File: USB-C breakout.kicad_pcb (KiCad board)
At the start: 2 copper layers, 14.7 x 21.2 mm, 10 parts, among them J1 USB_C_Receptacle_USB2.0, P1 Conn_01x04_MountingPin

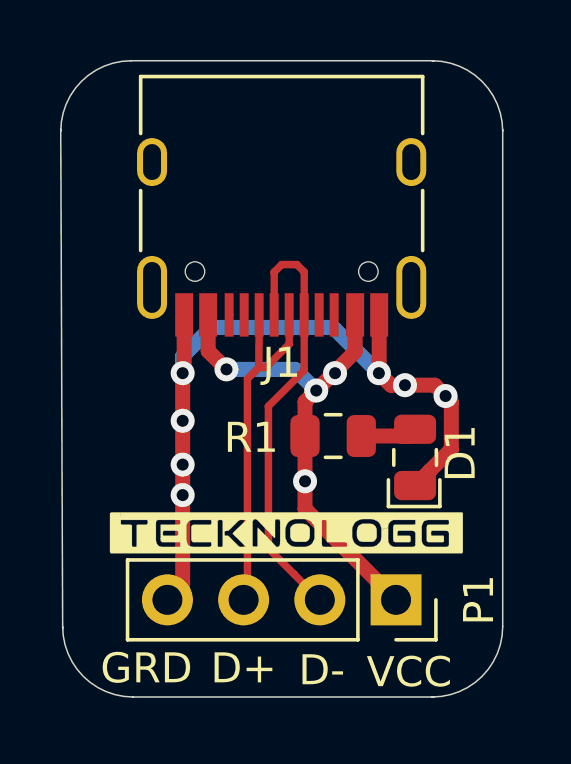
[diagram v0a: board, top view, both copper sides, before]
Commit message: Add CC resistors
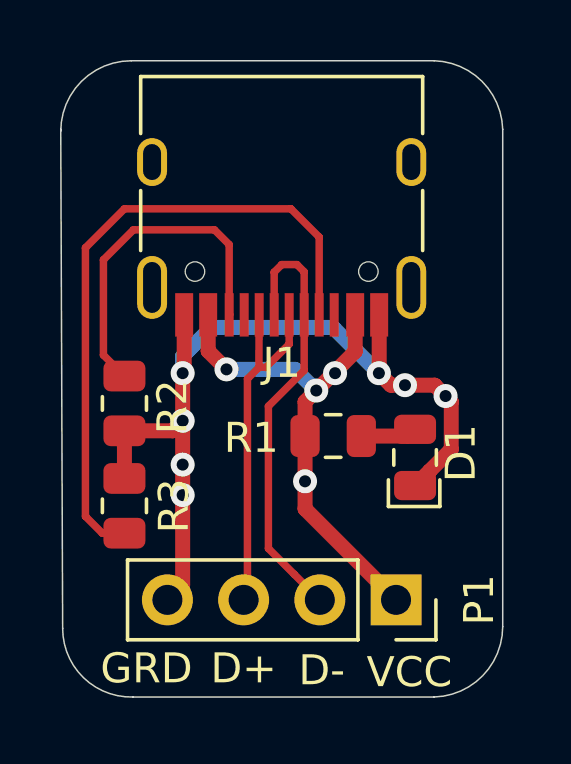
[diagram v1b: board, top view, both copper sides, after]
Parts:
- added R2: 5.11K, Resistor_SMD:R_0805_2012Metric, F.Cu at (107.8, 59.9)
- added R3: 5.11K, Resistor_SMD:R_0805_2012Metric, F.Cu at (107.8, 63.4)
- ?: moved to B.Cu
- turned ? to 180 degrees
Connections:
- J1 pad A8: Net-(J1-PadA8) -> unconnected-(J1-PadA8)
- J1 pad B8: Net-(J1-PadB8) -> unconnected-(J1-PadB8)
- J1 pad S1: Net-(J1-PadS1) -> unconnected-(J1-PadS1)
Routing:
- net Net-(J1-PadA5): track 0.00 -> 21.8 mm
- net Net-(J1-PadB5): track 0.03 -> 11.3 mm
- net GND: track 25.9 -> 29.6 mm
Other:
- net class Default removed
